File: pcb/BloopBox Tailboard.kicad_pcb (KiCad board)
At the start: 4 copper layers, 60 x 49 mm, 71 parts, among them J1 USB_C_Receptacle_Power, J2 Barrel_Jack, J3 Mainboard, J4 ICSP, Q1 AO3401A, Q3 AO3401A, Q5 AO3401A, SW1 Button2, SW2 Button1, U1 HT7533-1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

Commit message: feat: add and use versioning variables
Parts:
- added G***: LOGO, My_Footprints:CutieMark5mmInverted, B.Cu at (160.0, 69.8)
- added REF**: OSHW-Logo_7.5x8mm_SilkScreen, Symbol:OSHW-Logo_7.5x8mm_SilkScreen, B.Cu at (130.0, 70.5)
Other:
- board text added: "${TITLE} ${VERSION} ${DATE}"
- board text added: "qete.sh/el"
- board text removed: "BloopBox TailBoard"

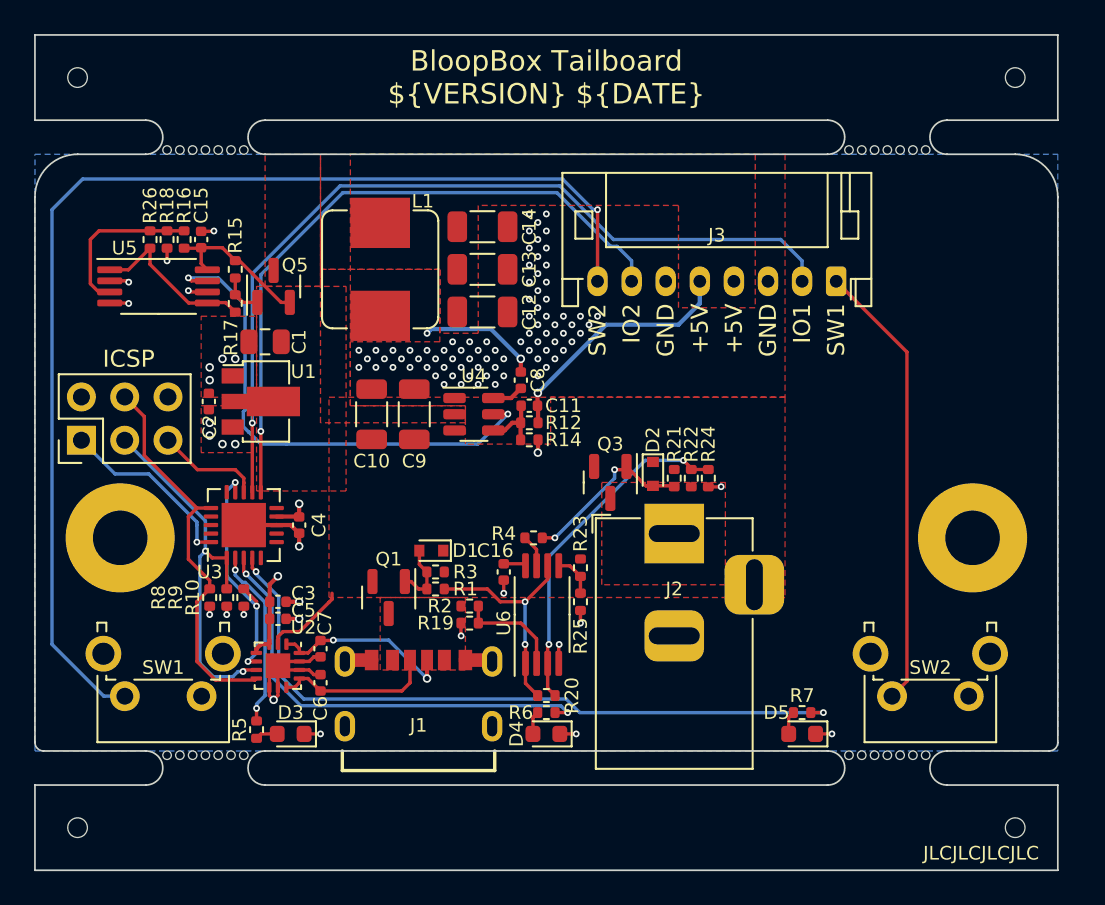
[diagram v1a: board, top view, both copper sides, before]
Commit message: fix!: remove Power Delivery circuitry
PD circuit was removed because it didn't work as planned in the current version and fixing it would make the board too expensive. The USB-C port is now hardwired to request 5V/3A.
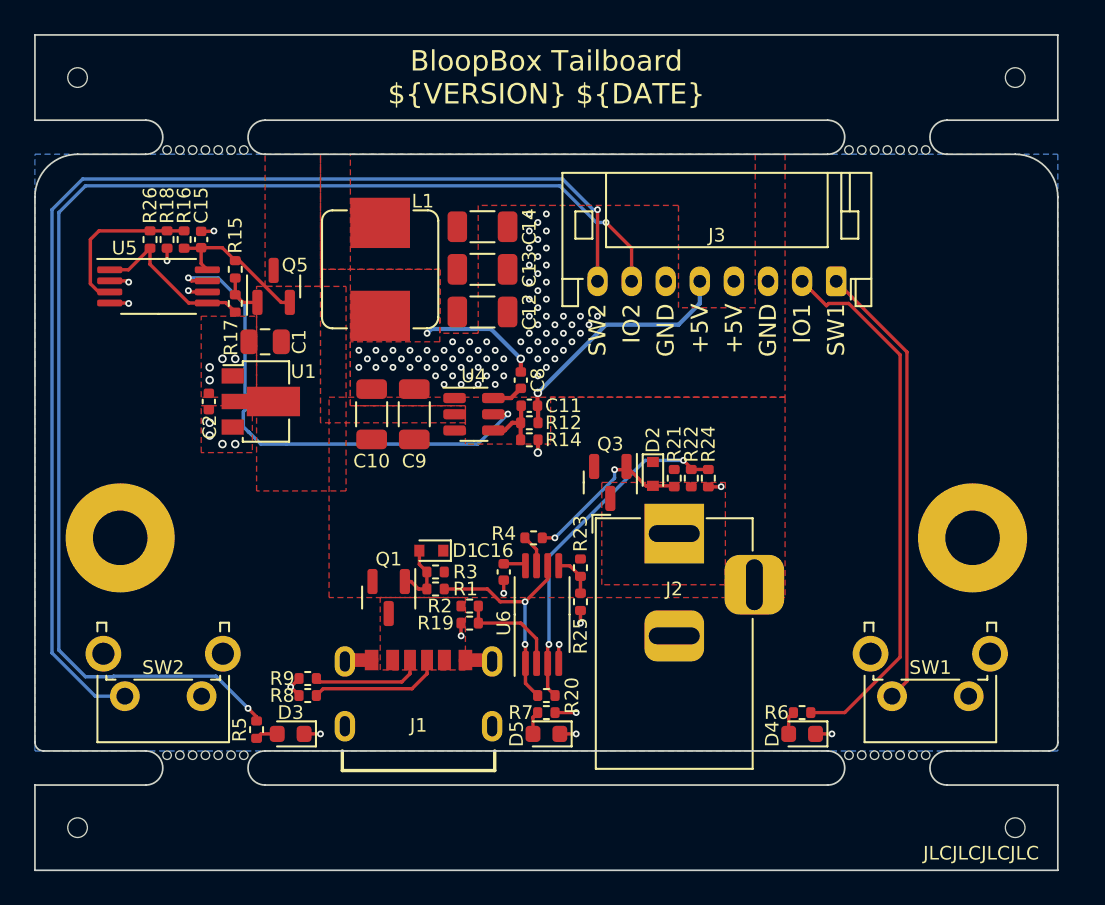
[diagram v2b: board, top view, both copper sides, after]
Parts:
- removed C3: 1uF, Capacitor_SMD:C_0402_1005Metric
- removed C4, C5: 100nF, Capacitor_SMD:C_0402_1005Metric
- removed C6, C7: 470pF, Capacitor_SMD:C_0402_1005Metric
- removed J4: ICSP, Connector_PinHeader_2.54mm:PinHeader_2x03_P2.54mm_Vertical
- removed R10: 4k7, Resistor_SMD:R_0402_1005Metric
- removed U2: FUSB302BMPX, Package_DFN_QFN:WQFN-14-1EP_2.5x2.5mm_P0.5mm_EP1.45x1.45mm
- removed U3: ATtiny24A-MU, Package_DFN_QFN:QFN-20-1EP_4x4mm_P0.5mm_EP2.6x2.6mm
- D3: value LED1 -> IO2
- D4: value LED2 -> IO1
- D5: value LED3 -> PWR
- R8, R9: value 4k7 -> 5k1
- SW1: value Button2 -> Button1
- SW2: value Button1 -> Button2
- moved SW1 45.0 mm to (169.8, 86.8)
- moved SW2 45.0 mm to (124.8, 86.8)
- moved D4 15.0 mm to (160.0, 89.0)
- moved D5 15.0 mm to (145.0, 89.0)
- moved R6 15.0 mm to (160.0, 87.8)
- moved R7 15.0 mm to (145.0, 87.8)
- moved R8 8.13 mm to (131.0, 86.8), turned to 180 degrees
- moved R9 6.72 mm to (131.0, 85.8), turned to 180 degrees
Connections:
- R5 pad 1: /PD-Controller/LED1 -> /IO2
- R6 pad 1: /PD-Controller/LED2 -> /IO1
- R7 pad 1: /PD-Controller/LED3 -> +3V3
- R8 pad 1: +3V3 -> /CC2
- R8 pad 2: /PD-Controller/SDA/MOSI -> GND
- R9 pad 1: +3V3 -> /CC1
- R9 pad 2: /PD-Controller/SCL/SCK -> GND
- SW1 pad 2: /Button2 -> /Button1
- SW2 pad 2: /Button1 -> /Button2
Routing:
- net /PD-Controller/LED3: track 41.1 -> 0.00 mm, vias 2 -> 0
- net /IO2: track 39.4 -> 76.9 mm, vias 1 -> 2
- net /PD-Controller/LED2: track 26.6 -> 0.00 mm, vias 2 -> 0
- net /PD-Controller/SDA/MOSI: track 23.1 -> 0.00 mm
- net /PD-Controller/SCL/SCK: track 22.0 -> 0.00 mm, vias 2 -> 0
- net /IO1: track 50.2 -> 32.0 mm, vias 1 -> 0
- net GND: track 29.6 -> 15.0 mm, vias 101 -> 98
- net /PD-Controller/~{INT}: track 14.0 -> 0.00 mm, vias 3 -> 0
- net /PD-Controller/MISO: track 10.8 -> 0.00 mm, vias 1 -> 0
- net /PD-Controller/LED1: track 10.6 -> 0.00 mm, vias 2 -> 0
- net +3V3: track 11.2 -> 3.53 mm, vias 11 -> 7
- net /PD-Controller/~{RESET}: track 6.23 -> 0.00 mm
- net VBUS: track 15.2 -> 10.3 mm
- net /CC2: track 10.9 -> 7.82 mm, vias 2 -> 0
- net /CC1: track 9.44 -> 6.57 mm

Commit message: fix: add missing LCSC part numbers
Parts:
- R16: value 13k -> 20k
- R18: value 22k -> 33k
